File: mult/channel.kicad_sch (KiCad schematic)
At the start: 9 parts, among them U1 OPA4197xPW

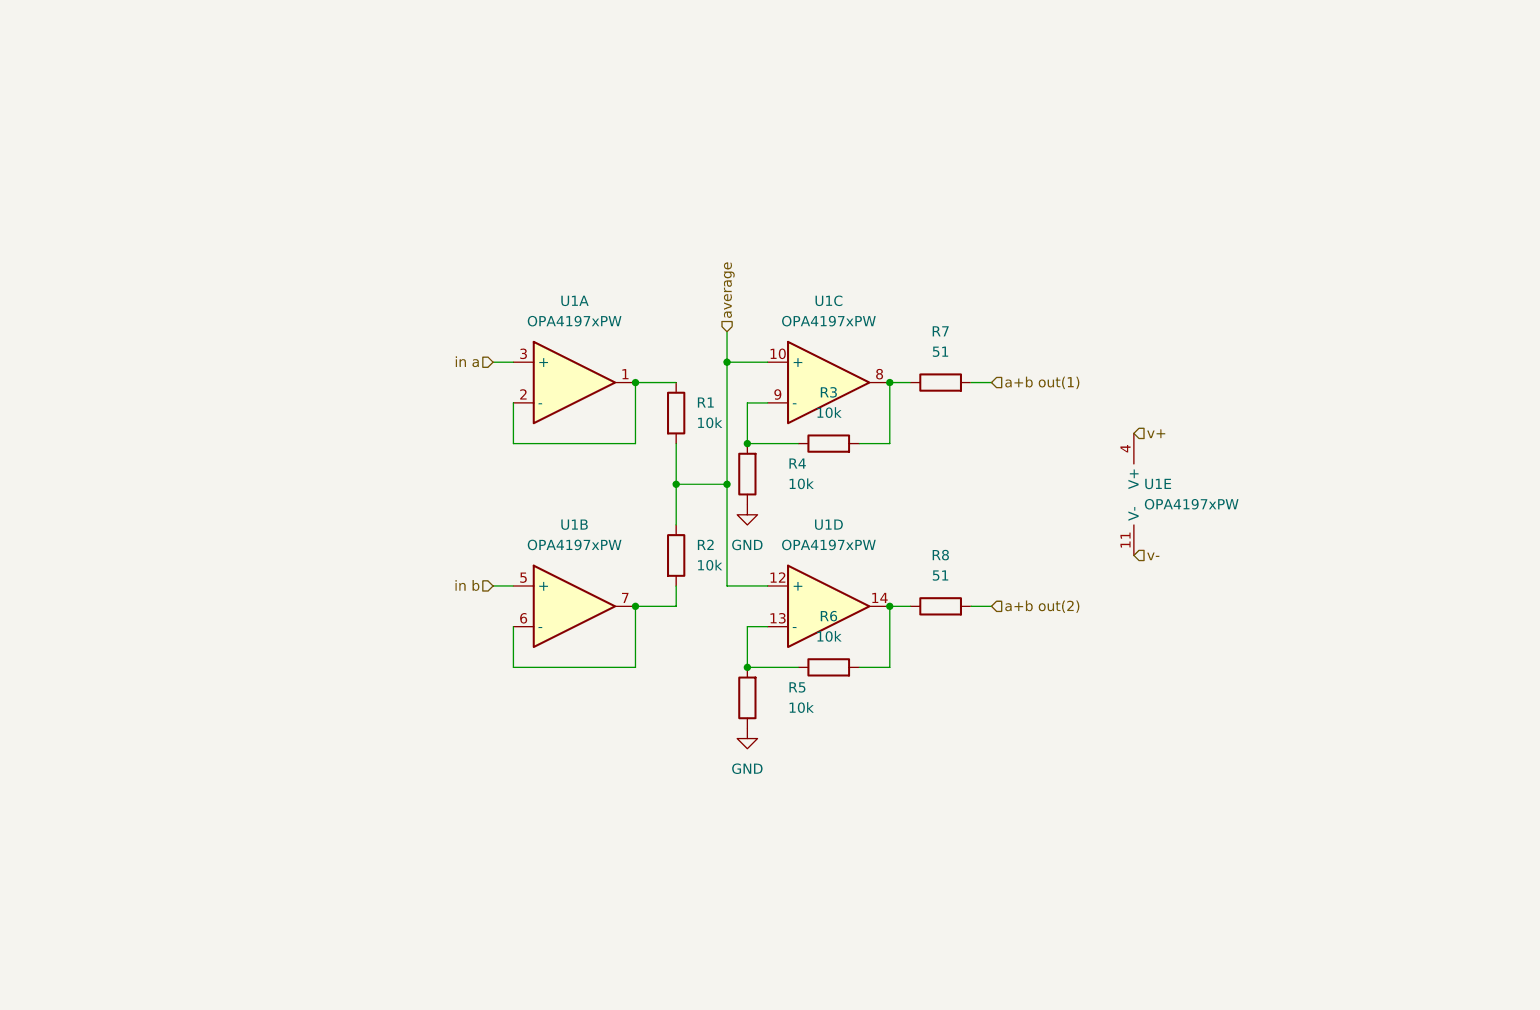
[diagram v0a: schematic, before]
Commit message: mult: Add jacks and bypass caps to channel
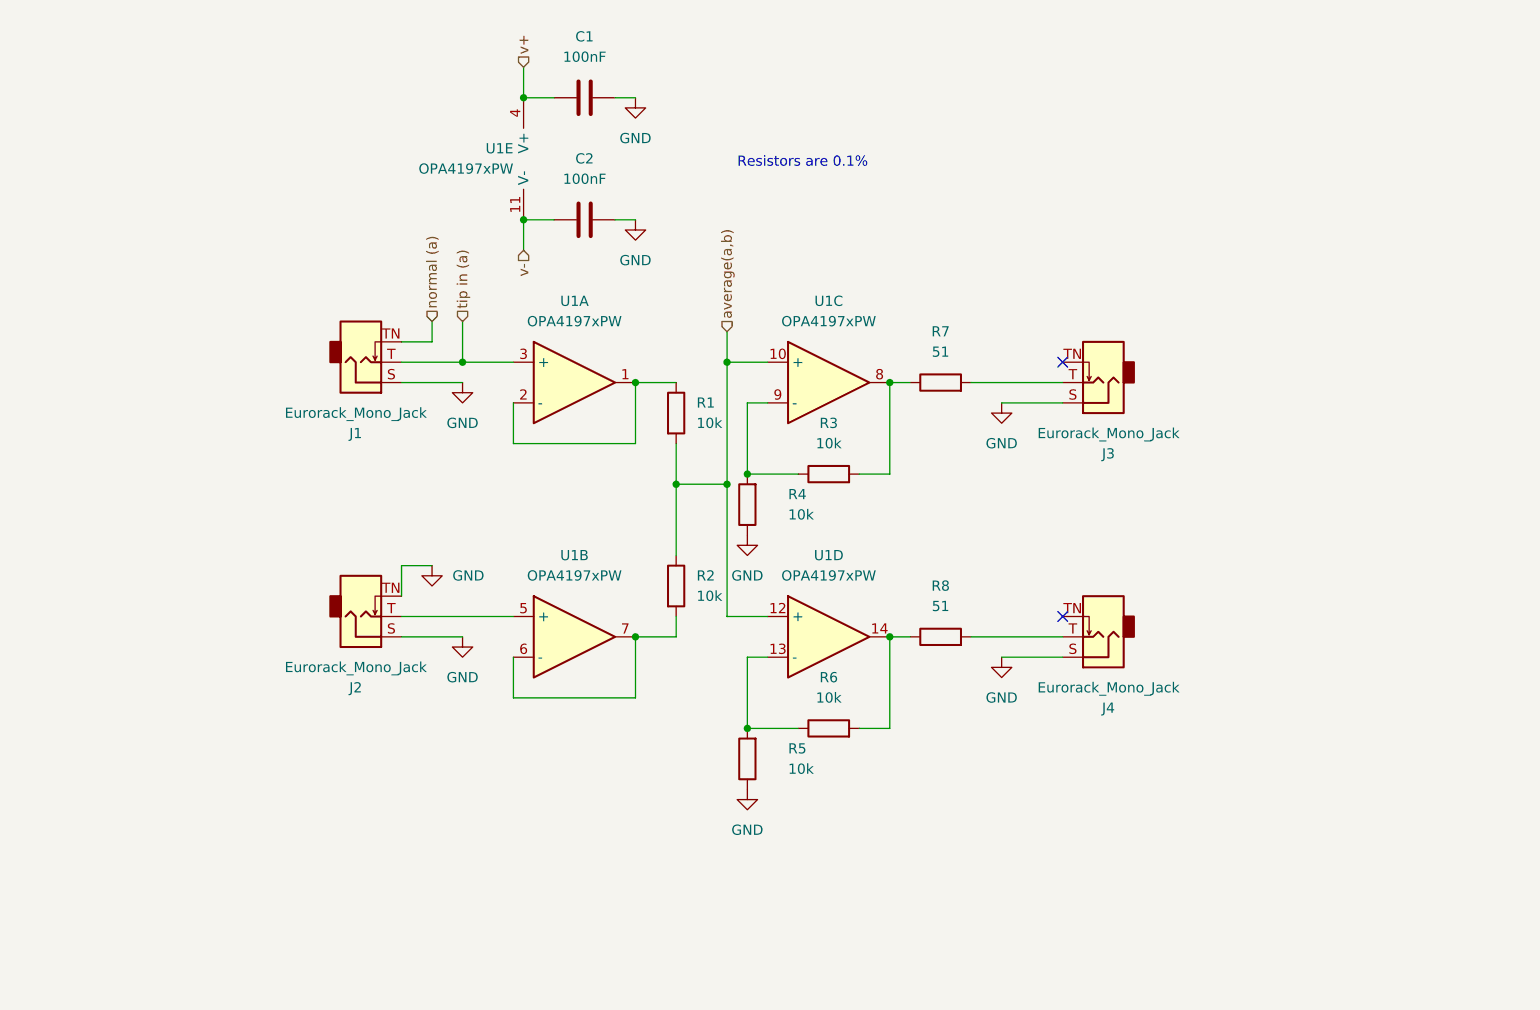
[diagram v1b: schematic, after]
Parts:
- added C1, C2: 100nF, symbol Device:C
- added J1, J2, J3, J4: Eurorack_Mono_Jack, winterbloom:AudioJack_WQP518MA, symbol winterbloom:Eurorack_Mono_Jack
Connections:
- net GND: now also C1.2, C2.2, J1.S (Sleeve), J2.S (Sleeve), J2.TN (Tip_normalize), J3.S (Sleeve), J4.S (Sleeve)
- net v+: now also C1.1
- net v-: now also C2.1
- net a+b out(1): no longer names the net of R7.2
- net a+b out(1): now also J3.T (Tip)
- net a+b out(2): no longer names the net of R8.2
- net a+b out(2): now also J4.T (Tip)
- net average renamed average(a,b)
- net in a renamed tip in (a)
- net tip in (a): now also J1.T (Tip)
- net in b: no longer names the net of U1.5 (+)
- net in b: now also J2.T (Tip)
- new net normal (a): J1.TN (Tip_normalize)
- no-connect marks 0 -> 2
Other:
- note added: "Resistors are 0.1%"
- moved on the sheet: R2, R3, R4, R5, R6, R8, U1B, U1D, U1E

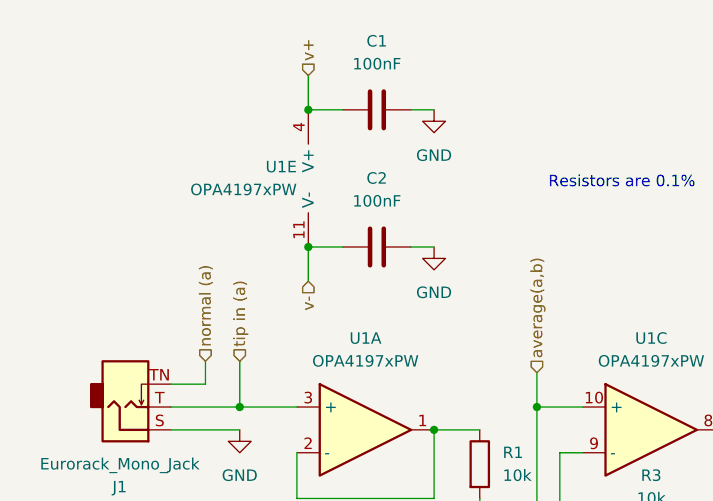
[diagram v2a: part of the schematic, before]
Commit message: mult: Replace v+ and v- labels with VCC,VEE
This removes a lot of unnecessary wires as well. Also updating LED
resistors to 1k to match Mutable Instruments Links and resolving TODO.
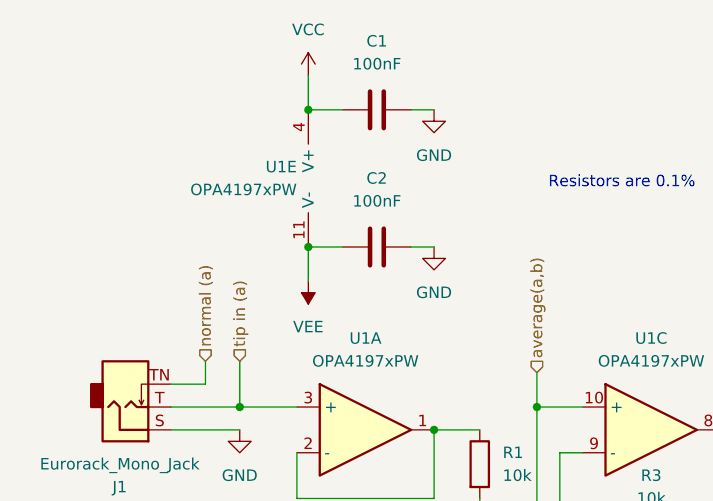
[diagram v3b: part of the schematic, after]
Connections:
- net v+ renamed VCC
- net v- renamed VEE
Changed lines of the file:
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@@
     (effects (font (size 1.27 1.27)) (justify left))
-  )
-  (hierarchical_label "v+" (shape input) (at 77.47 21.59 90) (fields_autoplaced)
-    (effects (font (size 1.27 1.27)) (justify left))
-  )
-  (hierarchical_label "v-" (shape input) (at 77.47 44.45 270) (fields_autoplaced)
-    (effects (font (size 1.27 1.27)) (justify right))
   )
   (hierarchical_label "normal (a)" (shape input) (at 66.04 53.34 90) (fields_autoplaced)
@@
     )
   )
+  (symbol (lib_id "power:VEE") (at 77.47 44.45 180) (unit 1)
+    (in_bom yes) (on_board yes) (dnp no) (fields_autoplaced)
+    (property "Reference" "#PWR049" (at 77.47 40.64 0)
+      (effects (font (size 1.27 1.27)) hide)
+    )
+    (property "Value" "VEE" (at 77.47 49.53 0)
+      (effects (font (size 1.27 1.27)))
+    )
+    (property "Footprint" "" (at 77.47 44.45 0)
+      (effects (font (size 1.27 1.27)) hide)
+    )
+    (property "Datasheet" "" (at 77.47 44.45 0)
+      (effects (font (size 1.27 1.27)) hide)
+    )
+    (pin "1")
+    (instances
+      (project "mult"
+        (path "/0e98ec4b-b4c7-447c-abd7-a761177a7f67/2249c80e-b931-4fee-ab04-d512ceb5f269"
+          (reference "#PWR049") (unit 1)
+        )
+        (path "/0e98ec4b-b4c7-447c-abd7-a761177a7f67/b290c7a8-131c-4f39-ab4f-62063cf2647f"
+          (reference "#PWR050") (unit 1)
+        )
+        (path "/0e98ec4b-b4c7-447c-abd7-a761177a7f67/b26d7339-1ce2-4103-8db8-9f6dbd3f09ef"
+          (reference "#PWR051") (unit 1)
+        )
+        (path "/0e98ec4b-b4c7-447c-abd7-a761177a7f67/c8627544-d82d-426a-84eb-b4928bf7d17c"
+          (reference "#PWR052") (unit 1)
+        )
+      )
+    )
+  )
   (symbol (lib_id "Device:R") (at 115.57 104.14 90) (unit 1)
     (in_bom yes) (on_board yes) (dnp no) (fields_autoplaced)
@@
         )
       )
+    )
+  )
+  (symbol (lib_id "power:VCC") (at 77.47 21.59 0) (unit 1)
+    (in_bom yes) (on_board yes) (dnp no) (fields_autoplaced)
+    (property "Reference" "#PWR045" (at 77.47 25.4 0)
+      (effects (font (size 1.27 1.27)) hide)
+    )
+    (property "Value" "VCC" (at 77.47 16.51 0)
+      (effects (font (size 1.27 1.27)))
+    )
+    (property "Footprint" "" (at 77.47 21.59 0)
+      (effects (font (size 1.27 1.27)) hide)
+    )
+    (property "Datasheet" "" (at 77.47 21.59 0)
+      (effects (font (size 1.27 1.27)) hide)
+    )
+    (pin "1")
+    (instances
+      (project "mult"
+        (path "/0e98ec4b-b4c7-447c-abd7-a761177a7f67/2249c80e-b931-4fee-ab04-d512ceb5f269"
+          (reference "#PWR045") (unit 1)
+        )
+        (path "/0e98ec4b-b4c7-447c-abd7-a761177a7f67/b290c7a8-131c-4f39-ab4f-62063cf2647f"
+          (reference "#PWR046") (unit 1)
+        )
+        (path "/0e98ec4b-b4c7-447c-abd7-a761177a7f67/b26d7339-1ce2-4103-8db8-9f6dbd3f09ef"
+          (reference "#PWR047") (unit 1)
+        )
+        (path "/0e98ec4b-b4c7-447c-abd7-a761177a7f67/c8627544-d82d-426a-84eb-b4928bf7d17c"
+          (reference "#PWR048") (unit 1)
+        )
+      )

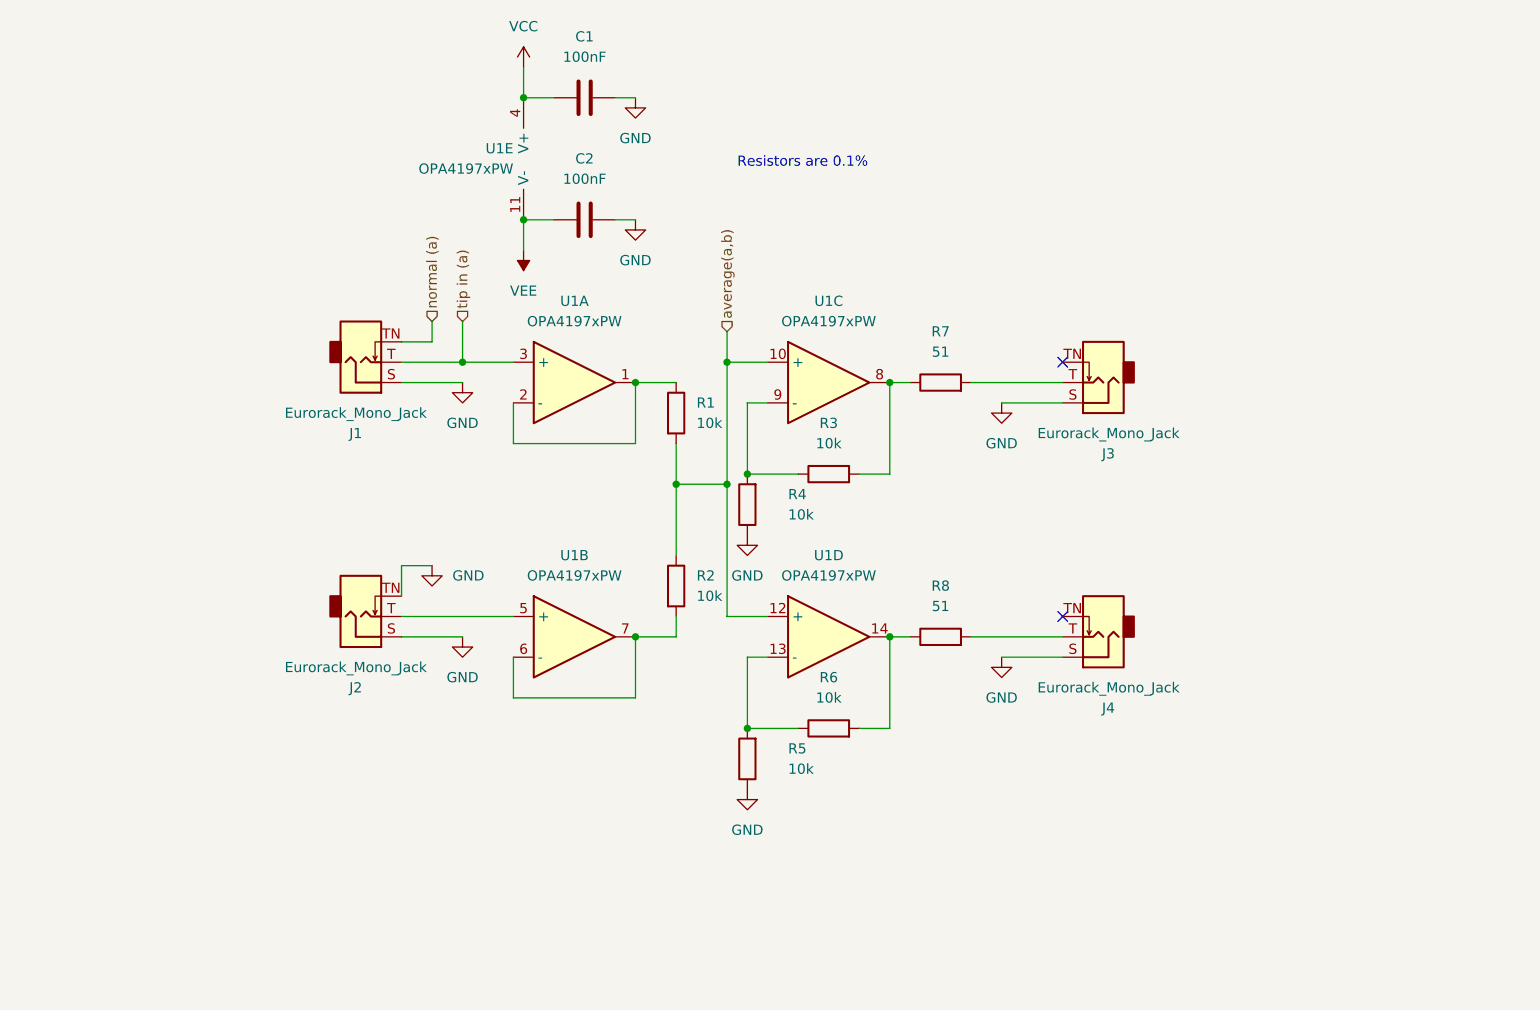
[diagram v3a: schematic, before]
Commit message: mult: Manually assign references, grouped by value
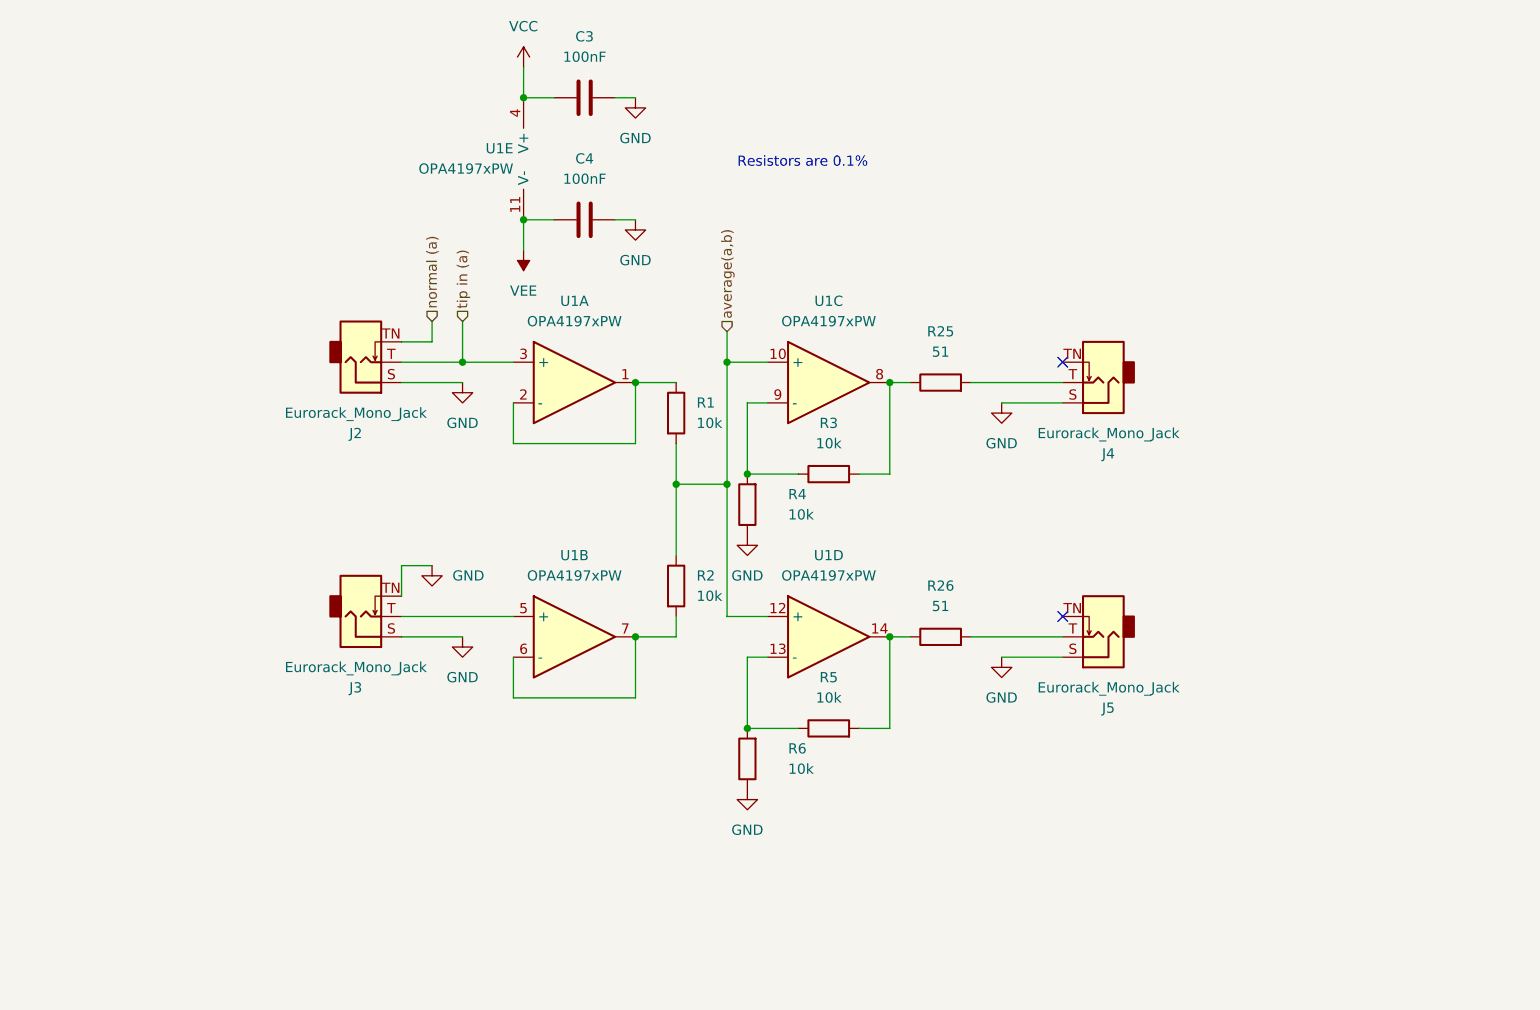
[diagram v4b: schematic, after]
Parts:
- renumbered C1 to C3, C2 to C4, J1 to J2, J2 to J3, J3 to J4, J4 to J5, R7 to R25, R8 to R26, R6 to R5, R5 to R6

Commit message: mult: Assign footprints
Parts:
- C3, C4: footprint (none) -> Capacitor_SMD:C_0805_2012Metric
- R1, R2, R25, R26, R3, R4, R5, R6: footprint (none) -> Resistor_SMD:R_0805_2012Metric
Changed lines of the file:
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@@
       (effects (font (size 1.27 1.27)))
     )
-    (property "Footprint" "" (at 88.9 39.6748 0)
+    (property "Footprint" "Capacitor_SMD:C_0805_2012Metric" (at 88.9 39.6748 0)
       (effects (font (size 1.27 1.27)) hide)
     )
@@
       (effects (font (size 1.27 1.27)) (justify left))
     )
-    (property "Footprint" "" (at 94.742 86.36 90)
+    (property "Footprint" "Resistor_SMD:R_0805_2012Metric" (at 94.742 86.36 90)
       (effects (font (size 1.27 1.27)) hide)
     )
@@
       (effects (font (size 1.27 1.27)))
     )
-    (property "Footprint" "" (at 129.54 62.738 90)
+    (property "Footprint" "Resistor_SMD:R_0805_2012Metric" (at 129.54 62.738 90)
       (effects (font (size 1.27 1.27)) hide)
     )
@@
       (effects (font (size 1.27 1.27)) (justify left))
     )
-    (property "Footprint" "" (at 94.742 64.77 90)
+    (property "Footprint" "Resistor_SMD:R_0805_2012Metric" (at 94.742 64.77 90)
       (effects (font (size 1.27 1.27)) hide)
     )
@@
       (effects (font (size 1.27 1.27)) (justify right))
     )
-    (property "Footprint" "" (at 107.188 76.2 90)
+    (property "Footprint" "Resistor_SMD:R_0805_2012Metric" (at 107.188 76.2 90)
       (effects (font (size 1.27 1.27)) hide)
     )
@@
       (effects (font (size 1.27 1.27)))
     )
-    (property "Footprint" "" (at 115.57 105.918 90)
+    (property "Footprint" "Resistor_SMD:R_0805_2012Metric" (at 115.57 105.918 90)
       (effects (font (size 1.27 1.27)) hide)
     )
@@
       (effects (font (size 1.27 1.27)))
     )
-    (property "Footprint" "" (at 88.9 24.4348 0)
+    (property "Footprint" "Capacitor_SMD:C_0805_2012Metric" (at 88.9 24.4348 0)
       (effects (font (size 1.27 1.27)) hide)
     )
@@
       (effects (font (size 1.27 1.27)))
     )
-    (property "Footprint" "" (at 129.54 94.488 90)
+    (property "Footprint" "Resistor_SMD:R_0805_2012Metric" (at 129.54 94.488 90)
       (effects (font (size 1.27 1.27)) hide)
     )
@@
       (effects (font (size 1.27 1.27)) (justify right))
     )
-    (property "Footprint" "" (at 107.188 107.95 90)
+    (property "Footprint" "Resistor_SMD:R_0805_2012Metric" (at 107.188 107.95 90)
       (effects (font (size 1.27 1.27)) hide)
     )
@@
       (effects (font (size 1.27 1.27)))
     )
-    (property "Footprint" "" (at 115.57 74.168 90)
-      (effects (font (size 1.27 1.27)) hide)
-    )
+    (property "Footprint" "Resistor_SMD:R_0805_2012Metric" (at 115.57 74.168 90)
+      (effects (font (size 1.27 1.27)) hide)
+    )
